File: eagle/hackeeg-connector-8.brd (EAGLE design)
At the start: 116.3 x 30.3 mm, 19 parts

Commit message: connected IN1-8N to AGND
- for cable noise reduction
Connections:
- removed net N$1: AGND.SIGNAL, ELECTRODE-CONNECTOR.5
- new net AGND: AGND.SIGNAL, ELECTRODE-CONNECTOR.10, ELECTRODE-CONNECTOR.12, ELECTRODE-CONNECTOR.14, ELECTRODE-CONNECTOR.16, ELECTRODE-CONNECTOR.18, ELECTRODE-CONNECTOR.20, ELECTRODE-CONNECTOR.22, ELECTRODE-CONNECTOR.4, ELECTRODE-CONNECTOR.5, ELECTRODE-CONNECTOR.6, ELECTRODE-CONNECTOR.8
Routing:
- net N$1: track 50.5 -> 0.00 mm
- net AGND: track 0.00 -> 50.5 mm
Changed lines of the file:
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@@
 </elements>
 <signals>
-<signal name="N$1">
-<contactref element="AGND" pad="SIGNAL"/>
-<contactref element="ELECTRODE-CONNECTOR" pad="5"/>
-<wire x1="67.31" y1="17.38" x2="67.31" y2="19.812" width="0.508" layer="16"/>
-<wire x1="67.31" y1="19.812" x2="68.453" y2="20.955" width="0.508" layer="16"/>
-<wire x1="68.453" y1="20.955" x2="98.425" y2="20.955" width="0.508" layer="16"/>
-<wire x1="98.425" y1="20.955" x2="102.87" y2="16.51" width="0.508" layer="16"/>
-<wire x1="102.87" y1="16.51" x2="102.87" y2="6.35" width="0.508" layer="16"/>
-</signal>
 <signal name="N$2">
 <contactref element="IN1P" pad="SIGNAL"/>
@@
 <vertex x="110.363" y="2.54" curve="-90"/>
 </polygon>
+<contactref element="ELECTRODE-CONNECTOR" pad="4"/>
+<contactref element="ELECTRODE-CONNECTOR" pad="6"/>
+<contactref element="ELECTRODE-CONNECTOR" pad="8"/>
+<contactref element="ELECTRODE-CONNECTOR" pad="10"/>
+<contactref element="ELECTRODE-CONNECTOR" pad="12"/>
+<contactref element="ELECTRODE-CONNECTOR" pad="14"/>
+<contactref element="ELECTRODE-CONNECTOR" pad="16"/>
+<contactref element="ELECTRODE-CONNECTOR" pad="18"/>
+<contactref element="ELECTRODE-CONNECTOR" pad="20"/>
+<contactref element="ELECTRODE-CONNECTOR" pad="22"/>
+<contactref element="AGND" pad="SIGNAL"/>
+<contactref element="ELECTRODE-CONNECTOR" pad="5"/>
+<wire x1="67.31" y1="17.38" x2="67.31" y2="19.812" width="0.508" layer="16"/>
+<wire x1="67.31" y1="19.812" x2="68.453" y2="20.955" width="0.508" layer="16"/>
+<wire x1="68.453" y1="20.955" x2="98.425" y2="20.955" width="0.508" layer="16"/>
+<wire x1="98.425" y1="20.955" x2="102.87" y2="16.51" width="0.508" layer="16"/>
+<wire x1="102.87" y1="16.51" x2="102.87" y2="6.35" width="0.508" layer="16"/>
 </signal>
 </signals>

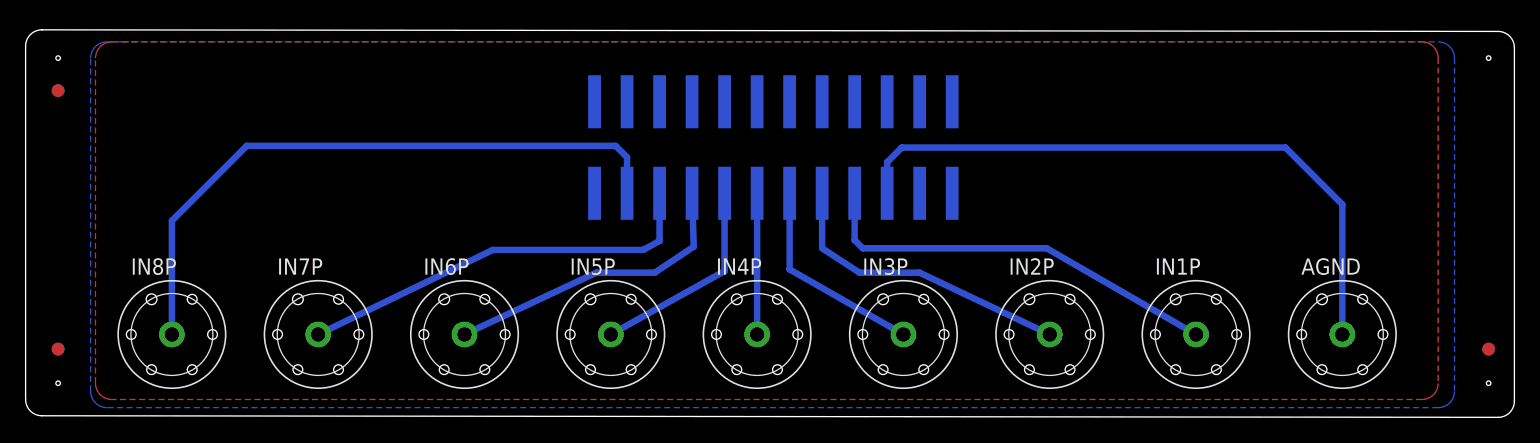
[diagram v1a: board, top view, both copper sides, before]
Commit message: reroute board with electrode conn on top
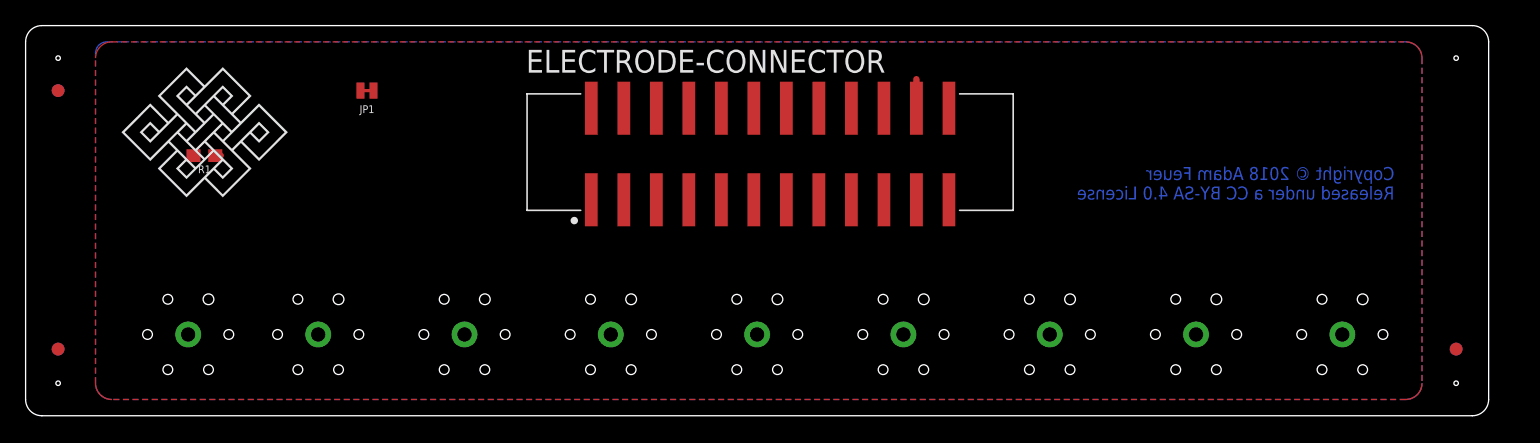
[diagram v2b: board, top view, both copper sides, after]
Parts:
- added JP1: JUMPER-SMT_2_NC_TRACE_NO-SILK, SparkFun-Jumpers:SMT-JUMPER_2_NC_TRACE_NO-SILK
- added R1: 0, SparkFun-Resistors:0603
- moved IN8P 91.4 mm to (102.9, 6.35), flipped to the bottom
- moved AGND 90.2 mm to (12.7, 6.35), flipped to the bottom
- moved IN1P 68.6 mm to (22.9, 6.35), flipped to the bottom
- moved IN7P 68.6 mm to (91.4, 6.35), flipped to the bottom
- moved IN2P 45.7 mm to (34.3, 6.35), flipped to the bottom
- moved IN6P 45.7 mm to (80.0, 6.35), flipped to the bottom
- moved IN3P 22.9 mm to (45.7, 6.35), flipped to the bottom
- moved IN5P 22.9 mm to (68.6, 6.35), flipped to the bottom
- moved U$1 5.03 mm to (14.1, 22.1), flipped to the top
- moved U$13 2.54 mm to (102.6, 22.4)
- moved FD3 2.54 mm to (111.8, 5.21)
- moved FD4 2.54 mm to (111.8, 5.21)
- moved ELECTRODE-CONNECTOR 0.57 mm to (58.2, 20.4), flipped to the top
- flipped IN4P to the bottom
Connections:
- new net AGND1: AGND.SIGNAL, ELECTRODE-CONNECTOR.5, R1.1
- new net N$17: JP1.1, R1.2
- net AGND: now also JP1.2; no longer AGND.SIGNAL, ELECTRODE-CONNECTOR.5
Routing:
- net N$9: track 50.1 -> 0.00 mm
- net AGND: track 50.5 -> 2.27 mm
- net N$2: track 32.4 -> 0.00 mm
- net N$8: track 32.1 -> 0.00 mm
- net N$7: track 23.8 -> 0.00 mm
- net N$3: track 23.7 -> 0.00 mm
- net N$6: track 16.3 -> 0.00 mm
- net N$4: track 16.2 -> 0.00 mm
- net N$5: track 11.0 -> 0.00 mm
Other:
- board size 116.3 x 30.3 mm -> 114.3 x 30.5 mm

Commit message: connector-8 as sent to macrofab initial run
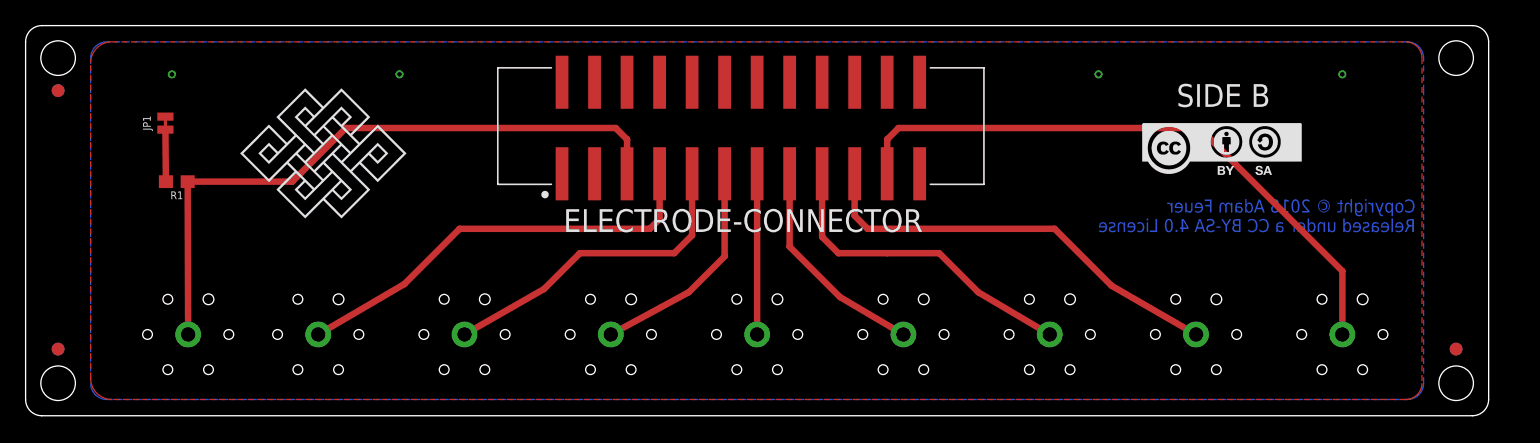
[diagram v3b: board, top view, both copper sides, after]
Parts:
- moved U$13 16.0 mm to (87.1, 18.5), flipped to the top
- moved JP1 16.0 mm to (10.9, 22.9), turned to 90 degrees
- moved U$1 9.42 mm to (23.4, 20.4)
- moved ELECTRODE-CONNECTOR 3.06 mm to (55.9, 22.5)
- moved R1 2.96 mm to (11.8, 18.3)
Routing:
- net AGND1: track 0.42 -> 51.1 mm
- net N$9: track 0.00 -> 48.2 mm
- net N$2: track 0.00 -> 33.4 mm
- net N$8: track 0.00 -> 33.2 mm
- net N$7: track 0.00 -> 25.4 mm
- net N$3: track 0.00 -> 25.3 mm
- net N$4: track 0.00 -> 17.3 mm
- net N$6: track 0.00 -> 17.0 mm
- net N$5: track 0.00 -> 12.6 mm
- net N$17: track 0.00 -> 4.06 mm
- net AGND: track 2.27 -> 0.00 mm, vias 0 -> 4
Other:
- board text added: "SIDE A"
- board text added: "SIDE B"
